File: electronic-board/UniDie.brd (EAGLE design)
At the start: 79.2 x 81.2 mm, 24 parts, among them IC1 ATMEGA88-THIN, J2 AVR_SPI_PROG_3X2NS

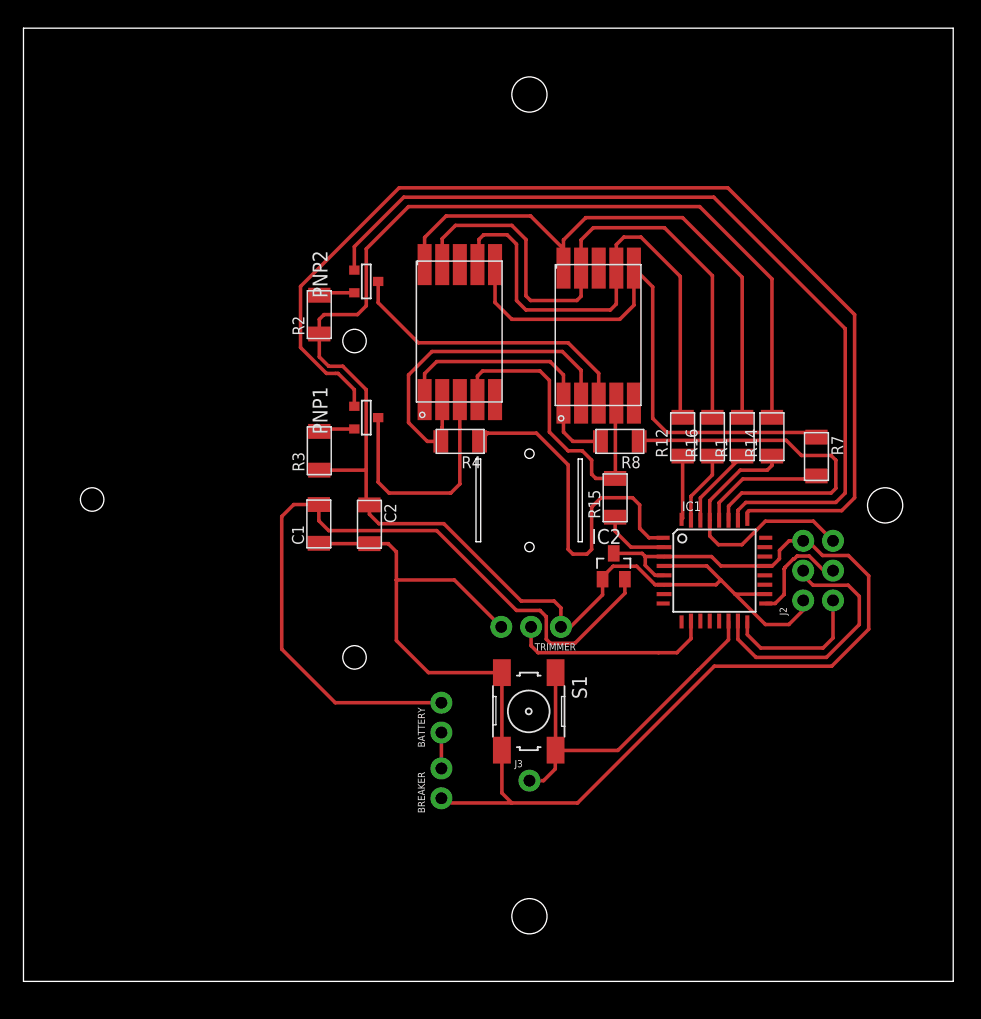
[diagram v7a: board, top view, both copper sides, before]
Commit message: Adapted parts and routes for milling. Prepared milling files
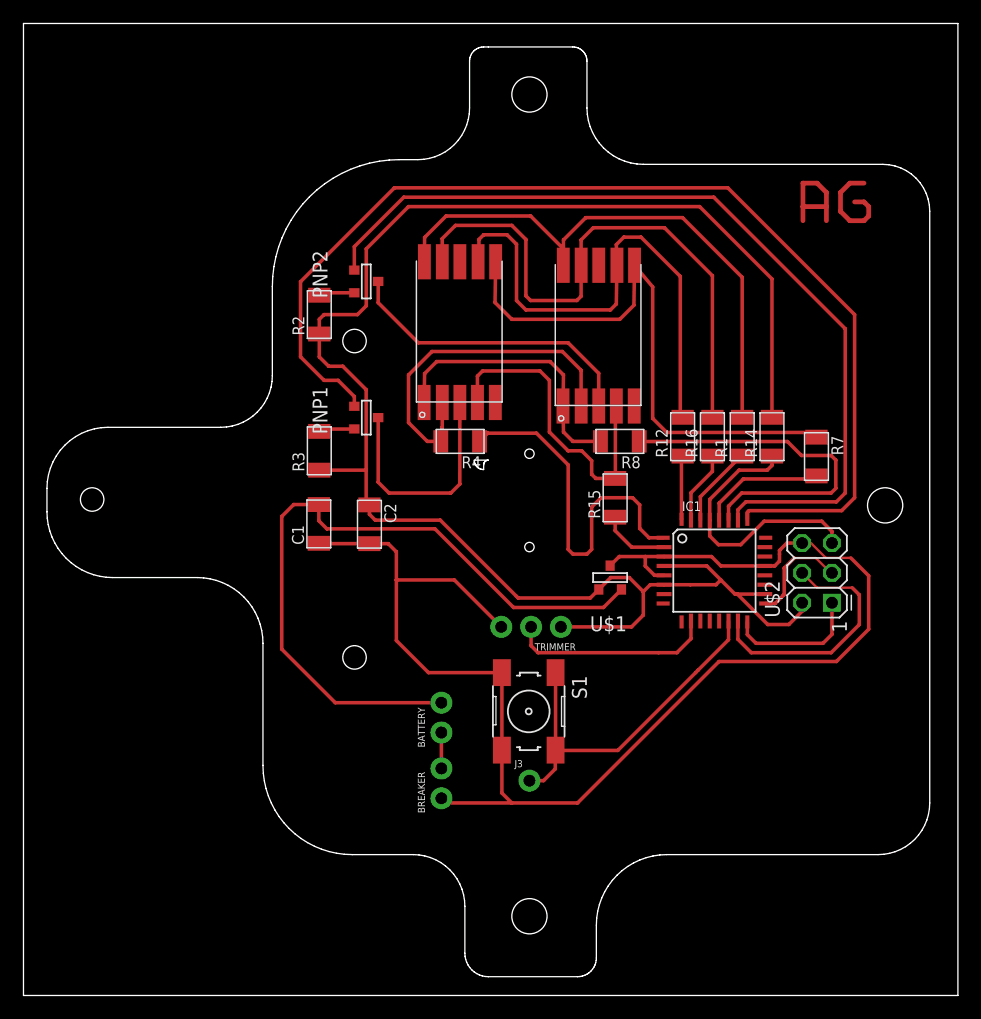
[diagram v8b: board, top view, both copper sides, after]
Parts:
- removed IC2: (no value), fab:SOT23
- removed J2: AVR_SPI_PROG_3X2NS, SparkFun-Connectors:2X3-NS
- added U$1: 5V-REG, AG:SOT-23
- added U$2: AVRISP, fab:2X03
- 7-SEG-LED1, 7-SEG-LED2: value (none) -> LDS-SMHTA304RISITR
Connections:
- net 5V: now also U$1.3, U$2.2; no longer IC2.1, J2.2
- net GND: now also U$1.1, U$2.6; no longer IC2.3, J2.6
- net MISO: now also U$2.1; no longer J2.1
- net MOSI: now also U$2.4; no longer J2.4
- net N$1: now also U$1.2; no longer IC2.2
- net RST: now also U$2.5; no longer J2.5
- net SCK: now also U$2.3; no longer J2.3
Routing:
- net N$11: track 0.00 -> 9.93 mm
- net N$12: track 0.00 -> 8.99 mm
- net N$1: track 66.2 -> 61.2 mm
- net 5V: track 139.3 -> 144.1 mm
- net MISO: track 12.4 -> 11.6 mm
- net SEG10: track 50.1 -> 49.4 mm
- net SEG6: track 47.6 -> 48.2 mm
- net RST: track 22.7 -> 23.3 mm
- net GND: track 121.3 -> 121.8 mm
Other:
- board size 79.2 x 81.2 mm -> 79.6 x 82.8 mm
